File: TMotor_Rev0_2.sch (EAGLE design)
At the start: 78 parts, among them J1 5015680507, J10 5015680207, J2 5015680507, J7 5015680207, J8 5015680207, J9 5015680207, U1 INA125U, U2 INA125U, U3 INA125U, U4 INA125U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

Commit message: added fuses and fets for motor power
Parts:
- removed FUSE: 0456020.ER, SamacSys_Parts:0456020.ER
- removed U$2, U$3, U$4, U$5: XT30PW-F, XT30PW-M:XT30PW-F
- added FUSE_L0, FUSE_L1, FUSE_R0, FUSE_R1: 0456020.ER, SamacSys_Parts:0456020.ER
- added L_0, L_1, R_0, R_1: XT30PW-F, XT30PW-M:XT30PW-F
- added Q1, Q2, Q3, Q4: IRLB8721PBFTO220H, IRLB8721PBF:IRLB8721PBFTO220H
- added U$6: 0458002.DR, SnapEDA-Library (1):0458002.DR
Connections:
- removed net PF_VCC: FUSE.1, R2.2, SHUNT.2
- new net L_0_ENABLE: Q1.G, U$1.26
- new net L_1_ENABLE: Q2.G, U$1.25
- new net N$43: FUSE_L0.2, L_0.+
- new net N$46: FUSE_L1.2, L_1.+
- new net N$47: FUSE_R1.2, R_1.+
- new net N$48: FUSE_R0.2, R_0.+
- new net N$49: L_0.-, Q1.D
- new net N$50: Q3.D, R_0.-
- new net N$51: Q4.D, R_1.-
- new net N$52: L_1.-, Q2.D
- new net R_0_ENABLE: Q3.G, U$1.8
- new net R_1_ENABLE: Q4.G, U$1.7
- new net VIN_PF: C23.2, FAN.1, U$1.VIN, U$6.P$2, USB.VIN
- net GND: now also Q1.S, Q2.S, Q3.S, Q4.S; no longer U$2.-, U$3.-, U$4.-, U$5.-
- net VCC: now also FUSE_L0.1, FUSE_L1.1, FUSE_R0.1, FUSE_R1.1, R2.2, SHUNT.2; no longer FUSE.2, U$2.+, U$3.+, U$4.+, U$5.+
- net VIN: now also U$6.P$1; no longer C23.2, FAN.1, U$1.VIN, USB.VIN

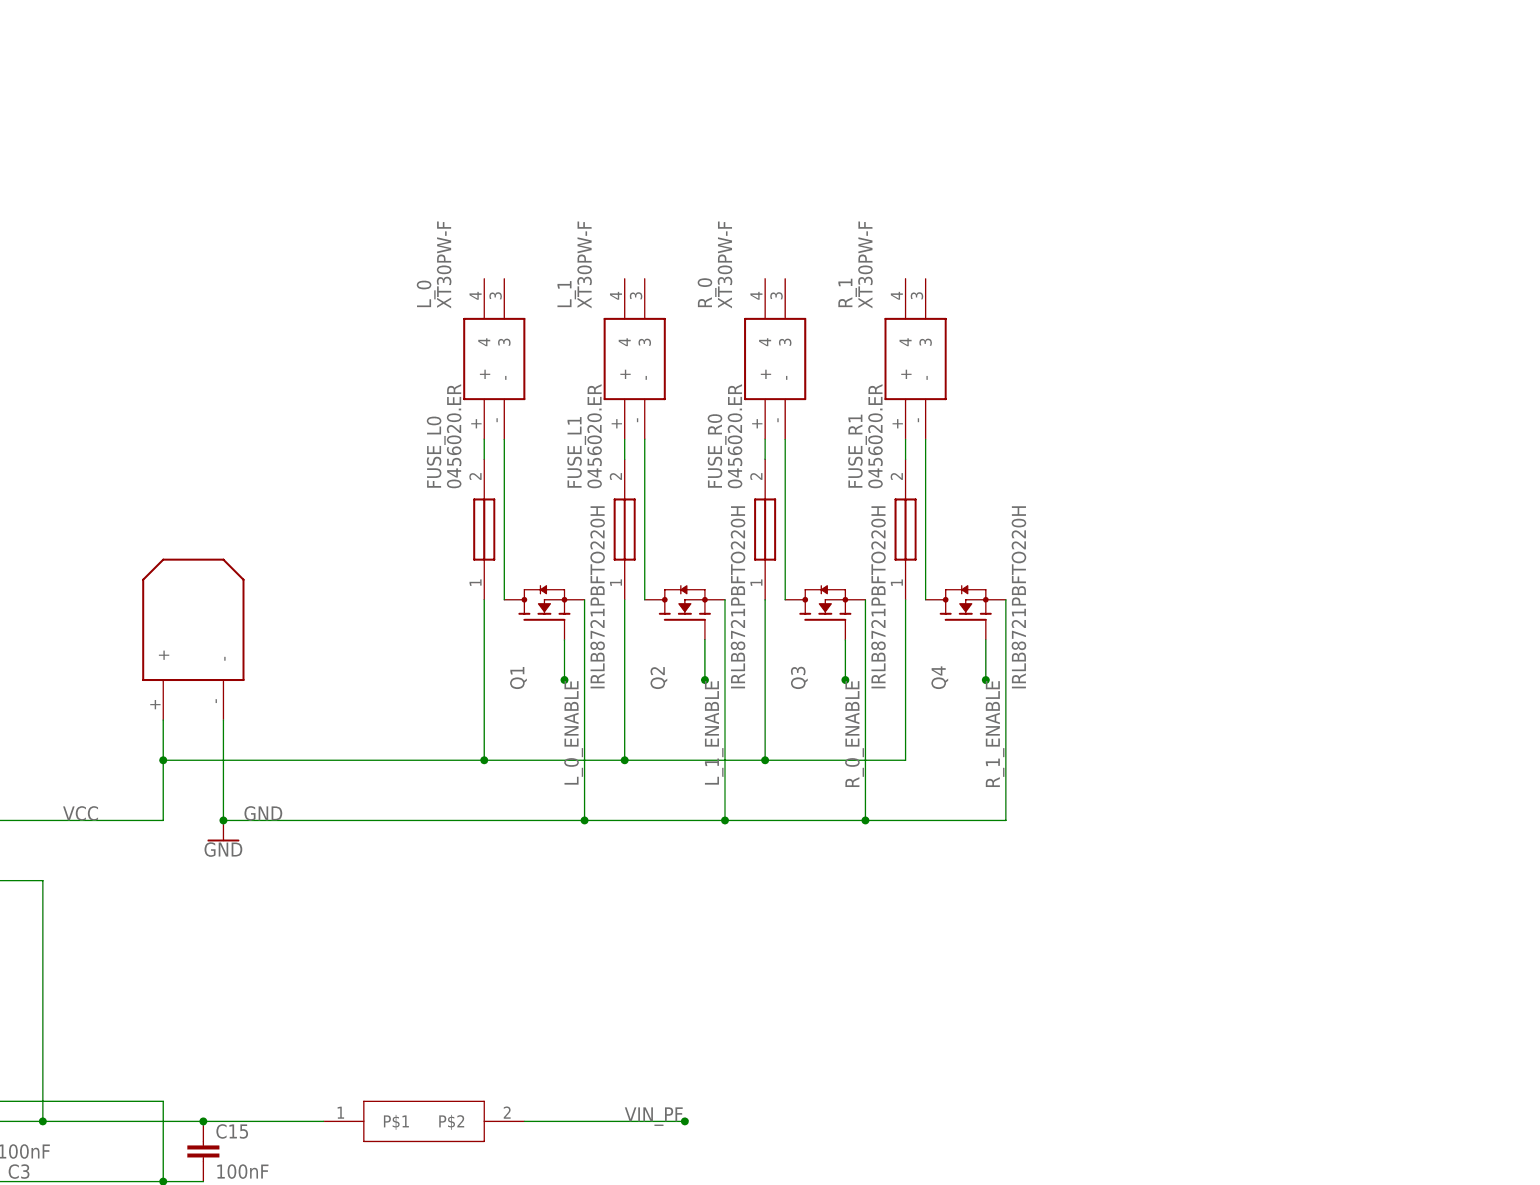
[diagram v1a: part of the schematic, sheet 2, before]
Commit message: Added Estop to motor power circuit
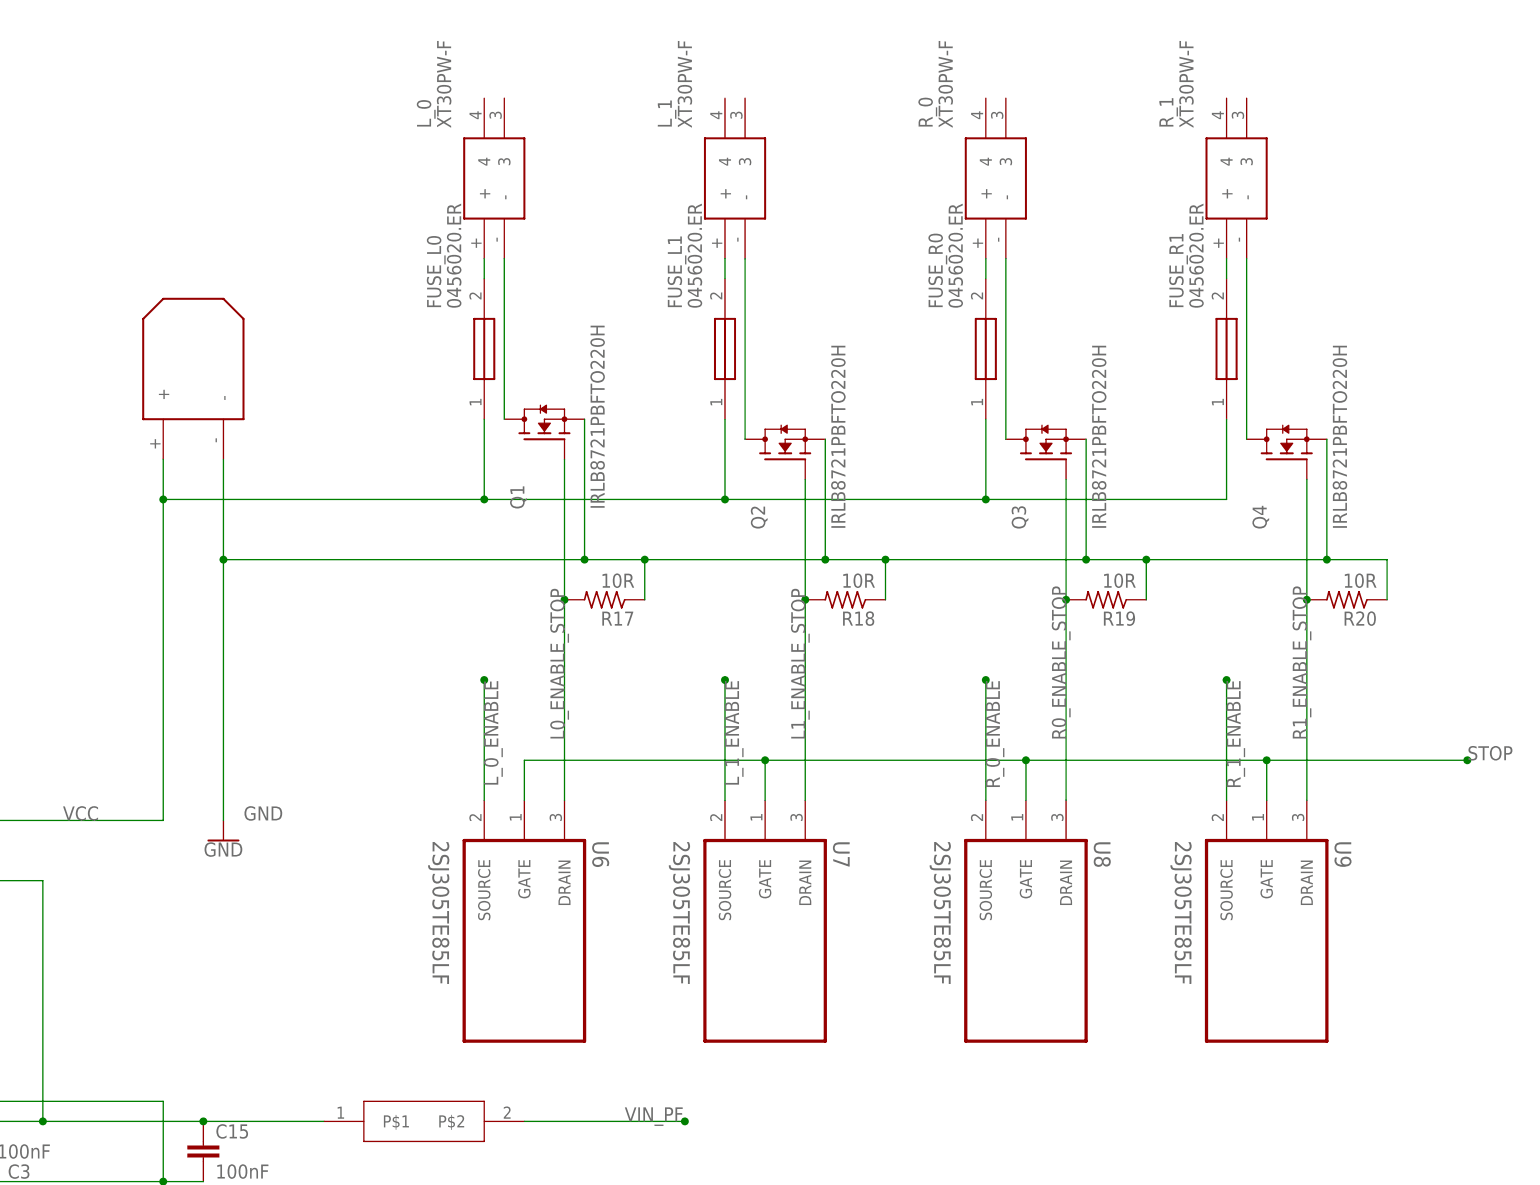
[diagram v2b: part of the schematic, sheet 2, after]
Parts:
- added R17, R18, R19, R20: 10R, rcl:R-US_0207/10
- added U6, U7, U8, U9: 2SJ305TE85LF, 2SJ305TE85LF:2SJ305TE85LF
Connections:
- new net L0_ENABLE_STOP: Q1.G, R17.2, U6.DRAIN
- new net L1_ENABLE_STOP: Q2.G, R18.2, U7.DRAIN
- new net R0_ENABLE_STOP: Q3.G, R19.2, U8.DRAIN
- new net R1_ENABLE_STOP: Q4.G, R20.2, U9.DRAIN
- net GND: now also R17.1, R18.1, R19.1, R20.1
- net L_0_ENABLE: now also U6.SOURCE; no longer Q1.G
- net L_1_ENABLE: now also U7.SOURCE; no longer Q2.G
- net R_0_ENABLE: now also U8.SOURCE; no longer Q3.G
- net R_1_ENABLE: now also U9.SOURCE; no longer Q4.G
- net STOP: now also U6.GATE, U7.GATE, U8.GATE, U9.GATE
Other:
- moved on the sheet: FUSE_L0, FUSE_L1, FUSE_R0, FUSE_R1, L_0, L_1, Q1, Q2, Q3, Q4, R_0, R_1

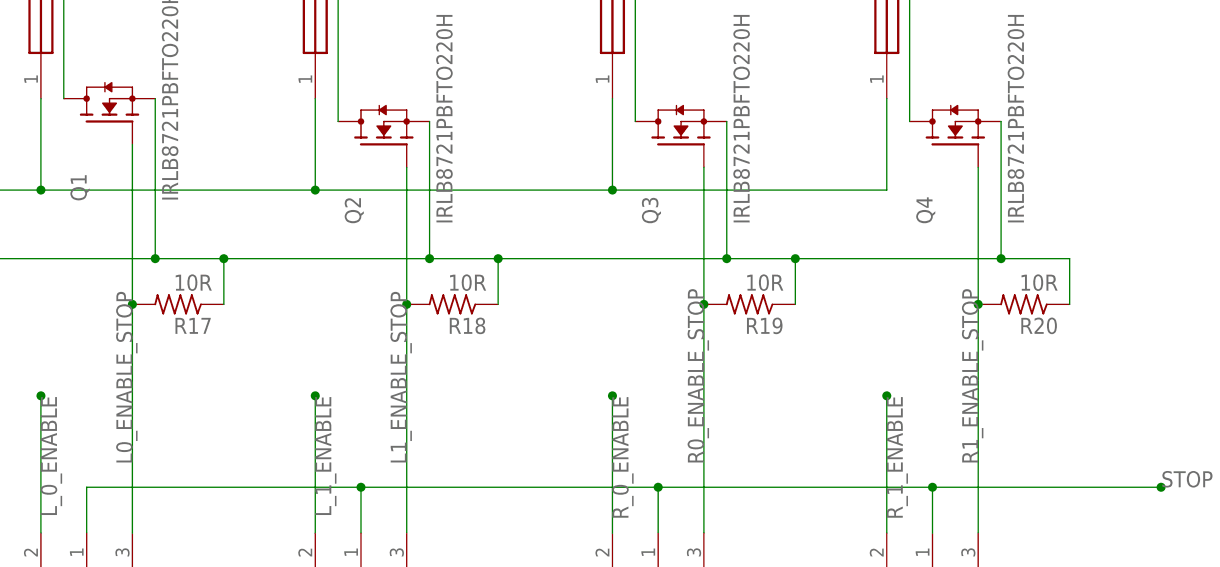
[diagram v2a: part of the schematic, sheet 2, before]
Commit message: Updated resistor value on motor stop pulldown
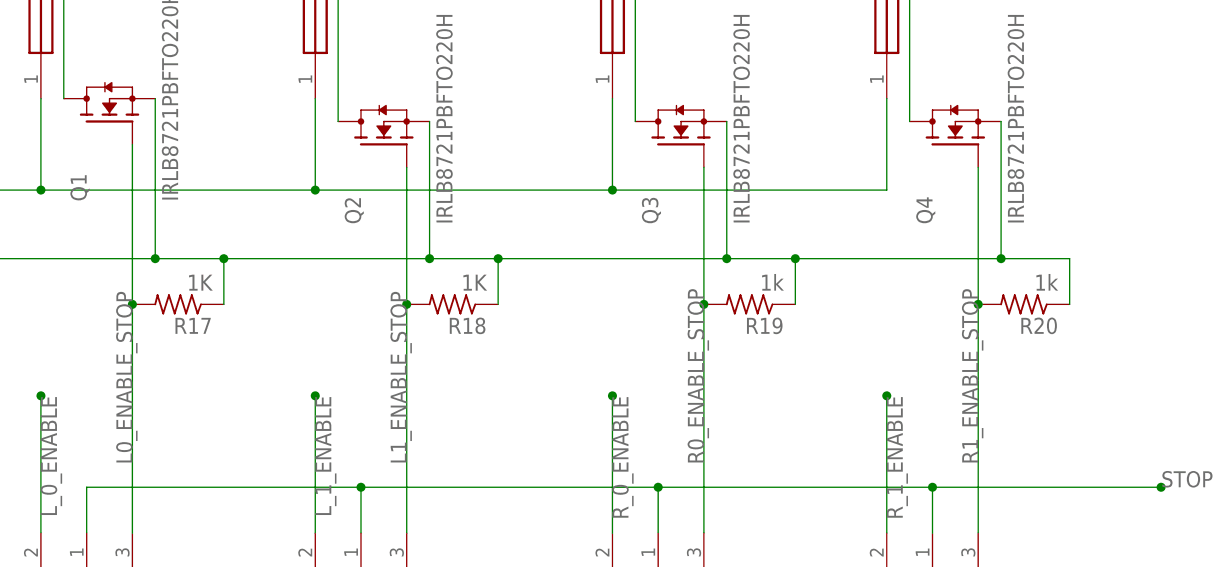
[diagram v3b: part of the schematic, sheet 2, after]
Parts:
- R17, R18: value 10R -> 1K
- R19, R20: value 10R -> 1k
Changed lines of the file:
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@@
 <part name="U8" library="2SJ305TE85LF" deviceset="2SJ305TE85LF" device=""/>
 <part name="U9" library="2SJ305TE85LF" deviceset="2SJ305TE85LF" device=""/>
-<part name="R17" library="rcl" library_urn="urn:adsk.eagle:library:334" deviceset="R-US_" device="0207/10" package3d_urn="urn:adsk.eagle:package:23491/2" value="10R"/>
-<part name="R18" library="rcl" library_urn="urn:adsk.eagle:library:334" deviceset="R-US_" device="0207/10" package3d_urn="urn:adsk.eagle:package:23491/2" value="10R"/>
-<part name="R19" library="rcl" library_urn="urn:adsk.eagle:library:334" deviceset="R-US_" device="0207/10" package3d_urn="urn:adsk.eagle:package:23491/2" value="10R"/>
-<part name="R20" library="rcl" library_urn="urn:adsk.eagle:library:334" deviceset="R-US_" device="0207/10" package3d_urn="urn:adsk.eagle:package:23491/2" value="10R"/>
+<part name="R17" library="rcl" library_urn="urn:adsk.eagle:library:334" deviceset="R-US_" device="0207/10" package3d_urn="urn:adsk.eagle:package:23491/2" value="1K"/>
+<part name="R18" library="rcl" library_urn="urn:adsk.eagle:library:334" deviceset="R-US_" device="0207/10" package3d_urn="urn:adsk.eagle:package:23491/2" value="1K"/>
+<part name="R19" library="rcl" library_urn="urn:adsk.eagle:library:334" deviceset="R-US_" device="0207/10" package3d_urn="urn:adsk.eagle:package:23491/2" value="1k"/>
+<part name="R20" library="rcl" library_urn="urn:adsk.eagle:library:334" deviceset="R-US_" device="0207/10" package3d_urn="urn:adsk.eagle:package:23491/2" value="1k"/>
 </parts>
 <sheets>
